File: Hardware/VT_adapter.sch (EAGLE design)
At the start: 14 parts

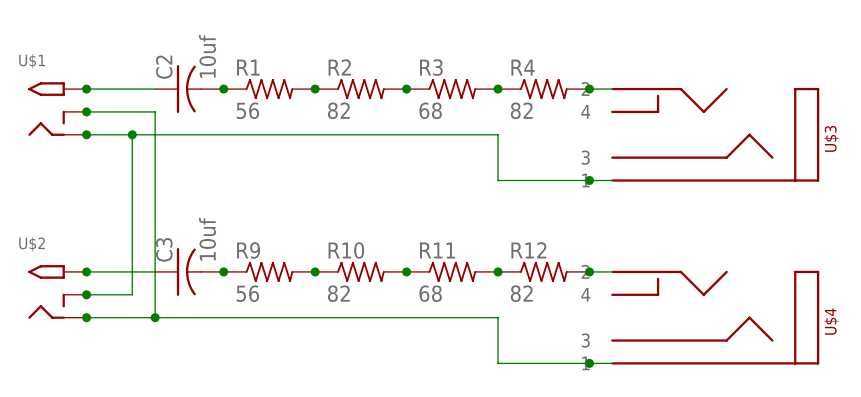
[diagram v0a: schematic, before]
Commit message: V2 adapter board
Use of this adapter requires removing burden resistor(s) from IoTaWatt.
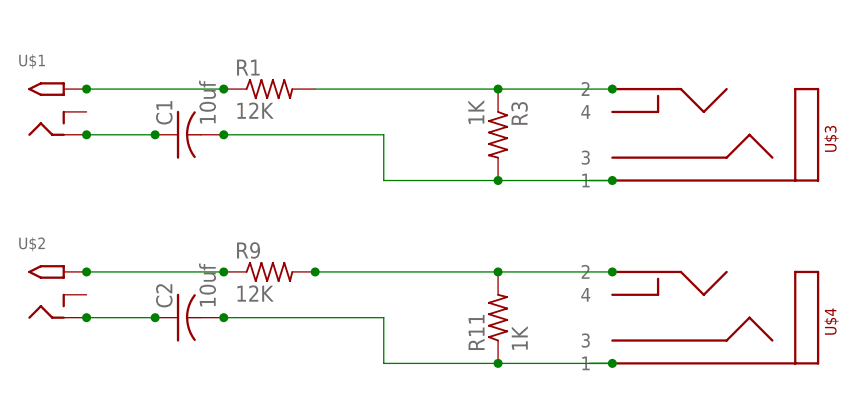
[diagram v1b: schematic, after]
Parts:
- removed C3: 10uf, resistor:C-USC0805
- removed R10, R12, R2, R4: 82, resistor:R-US_R1206
- added C1: 10uf, adafruit:C-USC1206
- C2: device resistor:C-USC0805 -> adafruit:C-USC1206
- R1, R9: value 56 -> 12K
- R11, R3: value 68 -> 1K
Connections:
- removed net N$10: R11.2, R12.1
- removed net N$13: C2.2, R1.1
- removed net N$14: C3.2, R9.1
- removed net N$5: R4.2, U$3.2
- removed net N$8: R10.1, R9.2
- removed net N$9: R10.2, R11.1
- net N$1: now also C1.2, R3.2, U$3.1; no longer C2.1, U$1.TIP
- net N$11: now also R11.2, R9.2; no longer R12.2
- net N$12: now also C2.2, R11.1; no longer U$1.RING_SW, U$2.RING
- net N$2: now also R3.1, U$3.2; no longer R2.1
- net N$3: now also C1.1, U$1.RING; no longer R2.2, R3.1
- net N$4: now also C2.1, U$2.RING; no longer R3.2, R4.1
- net N$6: now also R1.1, U$1.TIP; no longer U$1.RING, U$2.RING_SW, U$3.1
- net N$7: now also R9.1; no longer C3.1
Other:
- moved on the sheet: C2, R11, R3
